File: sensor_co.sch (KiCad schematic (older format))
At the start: 2 parts

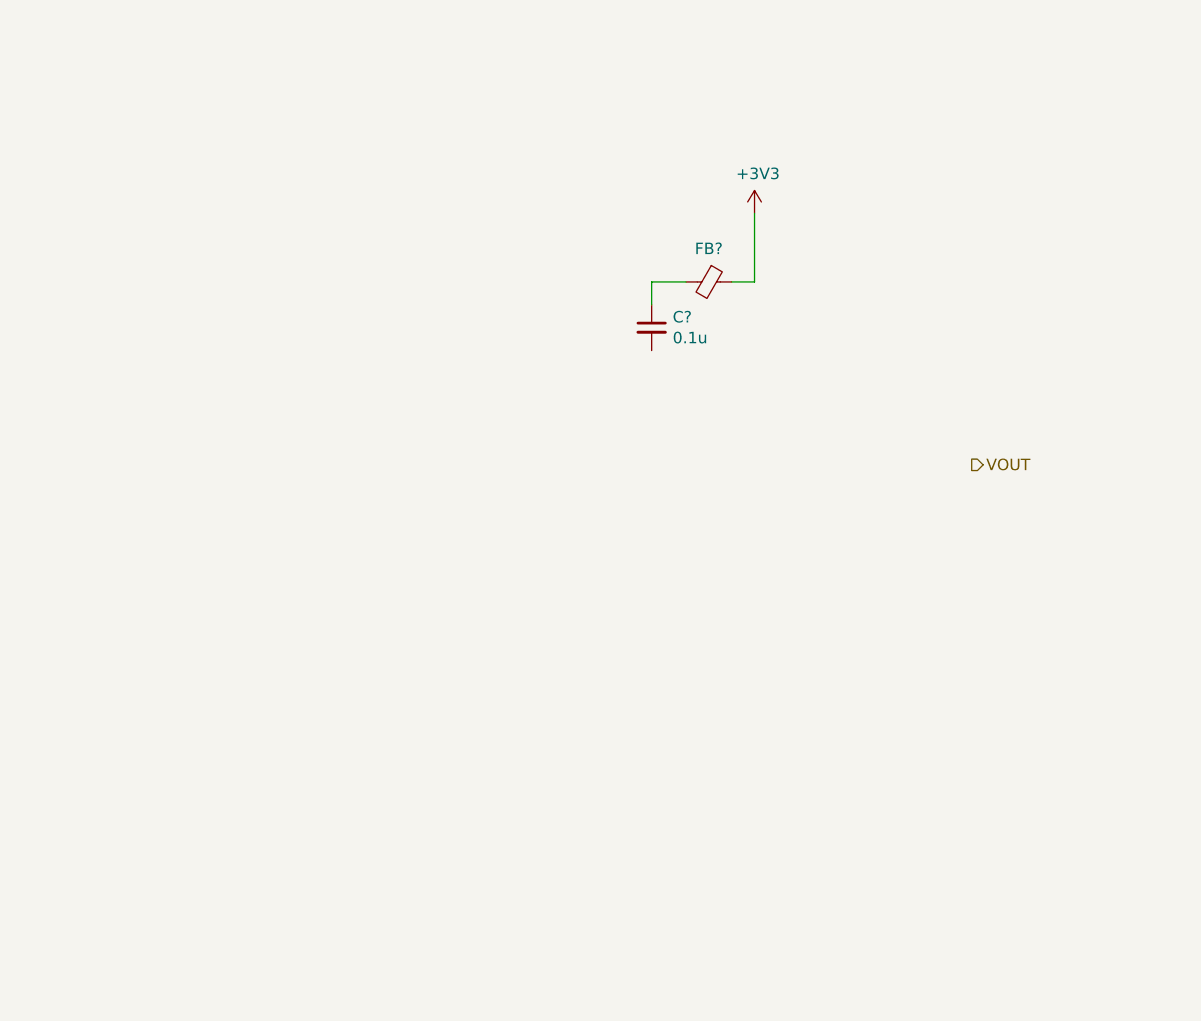
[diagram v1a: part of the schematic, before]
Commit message: Added CO sensor
Carbon Monoxide Sensor layout
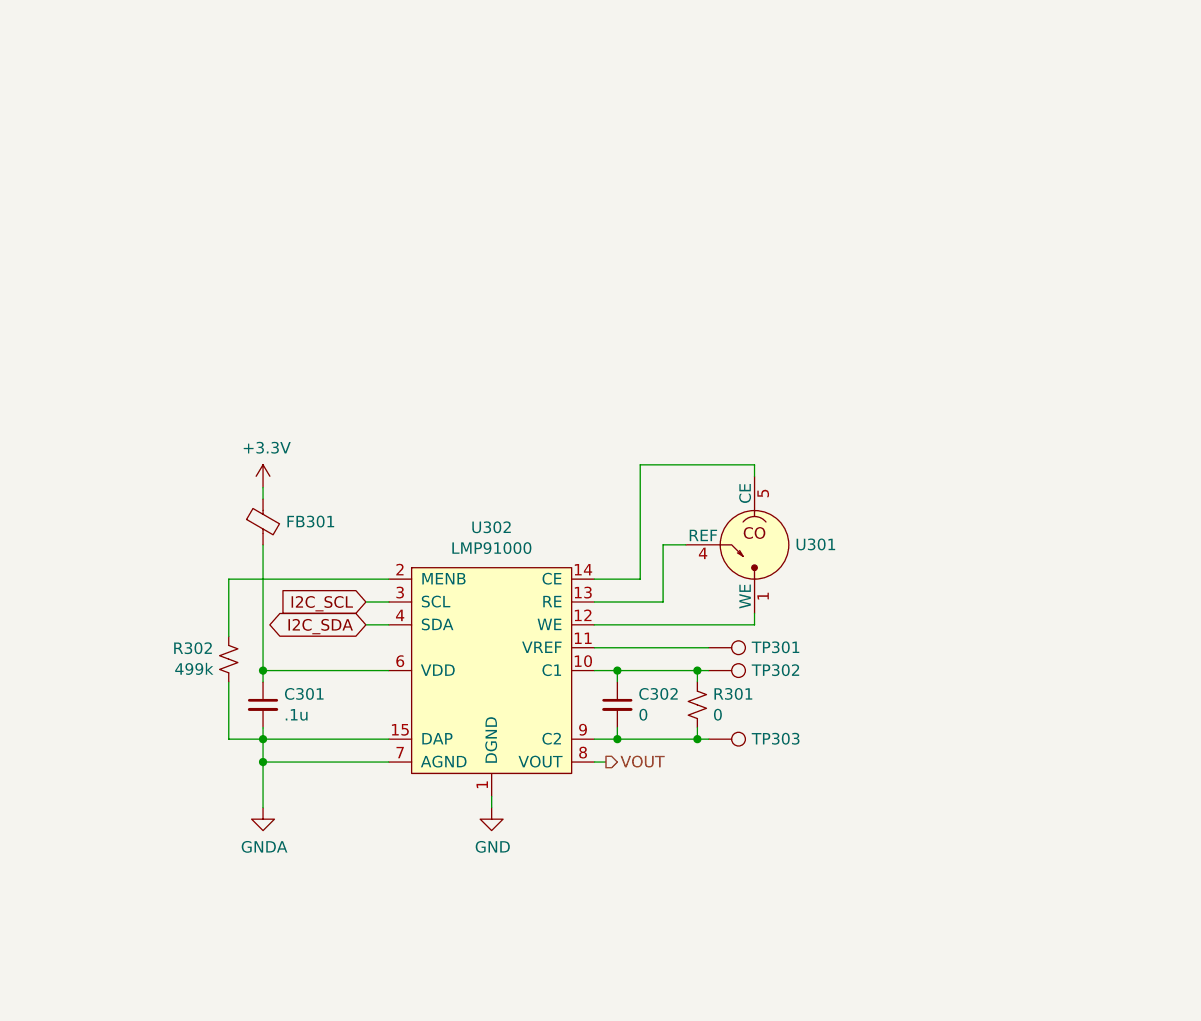
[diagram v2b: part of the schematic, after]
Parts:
- removed C?: 0.1u, Capacitor_SMD:C_0603_1608Metric, symbol Device:C_Small
- removed FB?: 470, Inductor_SMD:L_0603_1608Metric, symbol Device:Ferrite_Bead_Small
- added C301: .1u, Capacitor_SMD:C_0402_1005Metric, symbol Device:C_Small
- added C302: 0, Capacitor_SMD:C_0603_1608Metric, symbol Device:C_Small
- added FB301: Ferrite_Bead_Small, symbol Device:Ferrite_Bead_Small
- added R301: 0, Resistor_SMD:R_0603_1608Metric, symbol Device:R_Small_US
- added R302: 499k, Resistor_SMD:R_0603_1608Metric, symbol Device:R_Small_US
- added TP301, TP302, TP303: TestPoint, symbol Connector:TestPoint
- added U301: 110-102, mylib:SPEC_110-102, symbol mylib:110-102
- added U302: LMP91000, Package_SON:WSON-14-1EP_4.0x4.0mm_P0.5mm_EP2.6x2.6mm, symbol mylib:LMP91000
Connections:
- net +3V3: now also FB301.1
- net VOUT: now also U302.8 (VOUT)
- new net: C302.1, R301.1, TP302.1, U302.10 (C1)
- new net: TP301.1, U302.11 (VREF)
- new net: U301.1 (WE), U301.6 (WE), U302.12 (WE)
- new net: U301.4 (REF), U302.13 (RE)
- new net: U301.5 (CE), U302.14 (CE)
- new net: R302.1, U302.2 (MENB)
- new net: C301.1, FB301.2, U302.6 (VDD)
- new net: C302.2, R301.2, TP303.1, U302.9 (C2)
- new net: U301.2 (NC), U301.3 (NC)
- new net GND: U302.1 (DGND)
- new net GNDA: C301.2, R302.2, U302.15 (DAP), U302.7 (AGND)
- new net I2C_SCL: U302.3 (SCL)
- new net I2C_SDA: U302.4 (SDA)

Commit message: Minor part picking and annotation
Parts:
- FB301: footprint (none) -> Inductor_SMD:L_0603_1608Metric; Digikey (none) -> 490-5223-1-ND; MPN (none) -> BLM18PG471SN1D; Mouser (none) -> 81-BLM18PG471SN1D; Note (none) -> 470 Ohms @ 100MHz 1 Power Line Ferrite Bead 0603 1A 200mOhm
- TP301, TP302, TP303: DNP (none) -> 1
- U301: Digikey (none) -> 1684-1000-ND; MPN (none) -> 110-102; Manufacturer (none) -> SPEC Sensors, LLC
- U302: Digikey (none) -> 296-44382-1-ND; LCSC (none) -> C181364, C84366; MPN (none) -> LMP91000SD; Manufacturer (none) -> Texas Instruments; Note (none) -> IC AFE 1 CHAN 8BIT 14WSON
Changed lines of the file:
@@
 F 2 "Package_SON:WSON-14-1EP_4.0x4.0mm_P0.5mm_EP2.6x2.6mm" H 5600 3900 50  0001 C CNN
 F 3 "https://www.ti.com/lit/ds/symlink/lmp91000.pdf" H 5500 2950 50  0001 C CNN
+F 4 "296-44382-1-ND" H 5500 3450 50  0001 C CNN "Digikey"
+F 5 "C181364, C84366" H 5500 3450 50  0001 C CNN "LCSC"
+F 6 "LMP91000SD" H 5500 3450 50  0001 C CNN "MPN"
+F 7 "Texas Instruments" H 5500 3450 50  0001 C CNN "Manufacturer"
+F 8 "IC AFE 1 CHAN 8BIT 14WSON" H 5500 3450 50  0001 C CNN "Note"
 	1    5500 3450
 	1    0    0    -1
@@
 F 2 "mylib:SPEC_110-102" H 7150 3300 50  0001 C CNN
 F 3 "" H 6650 3100 50  0001 C CNN
+F 4 "1684-1000-ND" H 6650 3100 50  0001 C CNN "Digikey"
+F 5 "110-102" H 6650 3100 50  0001 C CNN "MPN"
+F 6 "SPEC Sensors, LLC" H 6650 3100 50  0001 C CNN "Manufacturer"
 	1    6650 3100
 	1    0    0    -1
@@
 F 2 "" H 6650 3550 50  0001 C CNN
 F 3 "~" H 6650 3550 50  0001 C CNN
+F 4 "1" H 6450 3550 50  0001 C CNN "DNP"
 	1    6450 3550
 	0    1    1    0
@@
 F 0 "FB301" H 4600 3000 50  0000 L CNN
 F 1 "Ferrite_Bead_Small" H 4600 2955 50  0001 L CNN
-F 2 "" V 4430 3000 50  0001 C CNN
+F 2 "Inductor_SMD:L_0603_1608Metric" V 4430 3000 50  0001 C CNN
 F 3 "~" H 4500 3000 50  0001 C CNN
+F 4 "490-5223-1-ND" H 4500 3000 50  0001 C CNN "Digikey"
+F 5 "BLM18PG471SN1D" H 4500 3000 50  0001 C CNN "MPN"
+F 6 "81-BLM18PG471SN1D " H 4500 3000 50  0001 C CNN "Mouser"
+F 7 "470 Ohms @ 100MHz 1 Power Line Ferrite Bead 0603 1A 200mOhm" H 4500 3000 50  0001 C CNN "Note"
 	1    4500 3000
 	1    0    0    -1
@@
 F 2 "" H 6650 3650 50  0001 C CNN
 F 3 "~" H 6650 3650 50  0001 C CNN
+F 4 "1" H 6450 3650 50  0001 C CNN "DNP"
 	1    6450 3650
 	0    1    1    0
@@
 F 2 "" H 6650 3950 50  0001 C CNN
 F 3 "~" H 6650 3950 50  0001 C CNN
+F 4 "1" H 6450 3950 50  0001 C CNN "DNP"
 	1    6450 3950
 	0    1    1    0

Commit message: Continue part picking
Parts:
- C301: value .1u -> 0.1u; footprint Capacitor_SMD:C_0402_1005Metric -> Capacitor_SMD:C_0603_1608Metric; Alt (none) -> .1u; Current (none) -> .1u; Description (none) -> .1u; Digikey 311-1336-1-ND -> 1292-1643-1-ND; Error 10% -> .1u; LCSC C129131 -> (none); MPN CC0402KRX5R6BB104 -> 0603B104K500CT; Mfr (none) -> .1u; Note CAP CER 0.1UF 10V X5R 0402 -> CAP CER 0.1UF 50V X7R 0603
- C302: DNP (none) -> 1
- FB301: LCSC (none) -> C97853
- TP301, TP302, TP303: footprint (none) -> TestPoint:TestPoint_Pad_D1.0mm
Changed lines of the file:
@@
 F 0 "TP301" V 6450 3738 50  0000 L CNN
 F 1 "TestPoint" V 6495 3738 50  0001 L CNN
-F 2 "" H 6650 3550 50  0001 C CNN
+F 2 "TestPoint:TestPoint_Pad_D1.0mm" H 6650 3550 50  0001 C CNN
 F 3 "~" H 6650 3550 50  0001 C CNN
 F 4 "1" H 6450 3550 50  0001 C CNN "DNP"
@@
 F 6 "81-BLM18PG471SN1D " H 4500 3000 50  0001 C CNN "Mouser"
 F 7 "470 Ohms @ 100MHz 1 Power Line Ferrite Bead 0603 1A 200mOhm" H 4500 3000 50  0001 C CNN "Note"
+F 8 "C97853" H 4500 3000 50  0001 C CNN "LCSC"
 	1    4500 3000
 	1    0    0    -1
@@
 P 4500 3800
 F 0 "C301" H 4592 3846 50  0000 L CNN
-F 1 ".1u" H 4592 3755 50  0000 L CNN
-F 2 "Capacitor_SMD:C_0402_1005Metric" H 4500 3800 50  0001 C CNN
-F 3 "~" H 4500 3800 50  0001 C CNN
-F 4 "311-1336-1-ND" H 4500 3800 50  0001 C CNN "Digikey"
-F 5 "10%" H 4500 3800 50  0001 C CNN "Error"
-F 6 "C129131" H 4500 3800 50  0001 C CNN "LCSC"
-F 7 "CC0402KRX5R6BB104" H 4500 3800 50  0001 C CNN "MPN"
-F 8 "CAP CER 0.1UF 10V X5R 0402" H 4500 3800 50  0001 C CNN "Note"
+F 1 "0.1u" H 4592 3755 50  0000 L CNN
+F 2 "Capacitor_SMD:C_0603_1608Metric" H 4500 3800 50  0001 C CNN
+F 3 ".1u" H 4500 3800 50  0001 C CNN
+F 4 "1292-1643-1-ND" H 4500 3800 50  0001 C CNN "Digikey"
+F 5 ".1u" H 4500 3800 50  0001 C CNN "Error"
+F 6 "" H 4500 3800 50  0001 C CNN "LCSC"
+F 7 "0603B104K500CT" H 4500 3800 50  0001 C CNN "MPN"
+F 8 "CAP CER 0.1UF 50V X7R 0603" H 4500 3800 50  0001 C CNN "Note"
+F 9 ".1u" H 4500 3800 50  0001 C CNN "Alt"
+F 10 ".1u" H 4500 3800 50  0001 C CNN "Current"
+F 11 ".1u" H 4500 3800 50  0001 C CNN "Description"
+F 12 ".1u" H 4500 3800 50  0001 C CNN "Mfr"
 	1    4500 3800
 	1    0    0    -1
@@
 F 0 "TP302" V 6450 3838 50  0000 L CNN
 F 1 "TestPoint" V 6495 3838 50  0001 L CNN
-F 2 "" H 6650 3650 50  0001 C CNN
+F 2 "TestPoint:TestPoint_Pad_D1.0mm" H 6650 3650 50  0001 C CNN
 F 3 "~" H 6650 3650 50  0001 C CNN
 F 4 "1" H 6450 3650 50  0001 C CNN "DNP"
@@
 F 0 "TP303" V 6450 4138 50  0000 L CNN
 F 1 "TestPoint" V 6495 4138 50  0001 L CNN
-F 2 "" H 6650 3950 50  0001 C CNN
+F 2 "TestPoint:TestPoint_Pad_D1.0mm" H 6650 3950 50  0001 C CNN
 F 3 "~" H 6650 3950 50  0001 C CNN
 F 4 "1" H 6450 3950 50  0001 C CNN "DNP"
@@
 F 2 "Capacitor_SMD:C_0603_1608Metric" H 6050 3800 50  0001 C CNN
 F 3 "~" H 6050 3800 50  0001 C CNN
+F 4 "1" H 6050 3800 50  0001 C CNN "DNP"
 	1    6050 3800
 	1    0    0    -1

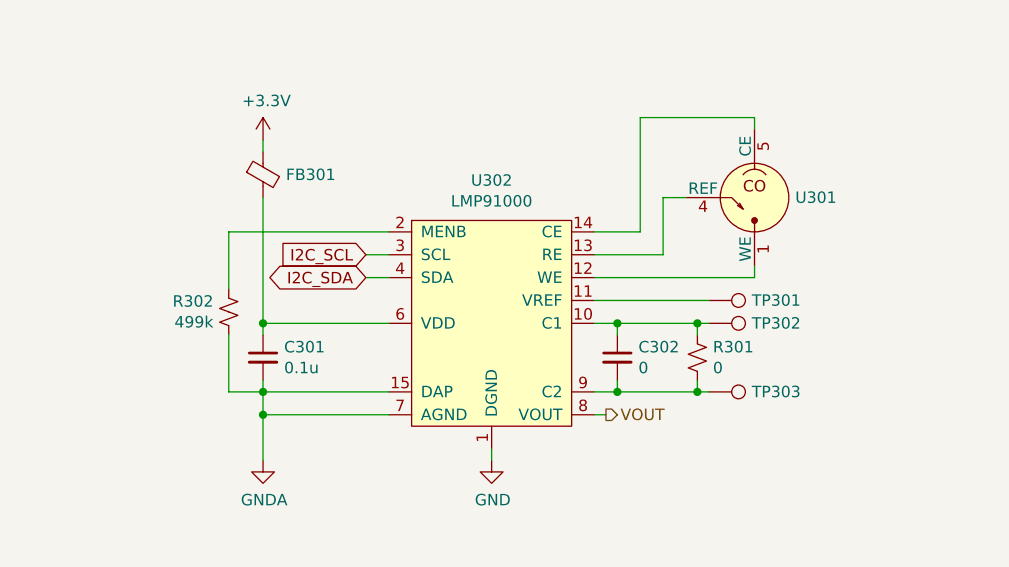
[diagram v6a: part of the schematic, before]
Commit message: Re-annotate all parts
Cleans up annotations
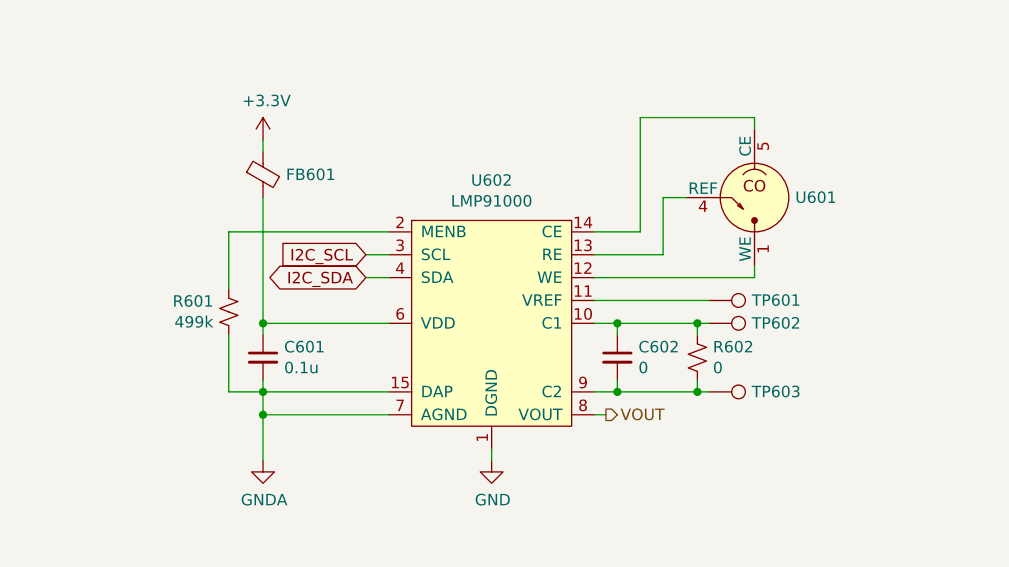
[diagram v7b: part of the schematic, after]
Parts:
- renumbered C301 to C601, C302 to C602, FB301 to FB601, R302 to R601, R301 to R602, TP301 to TP601, TP302 to TP602, TP303 to TP603, U301 to U601, U302 to U602
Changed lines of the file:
@@
 1) No external bias required for CO, thus no accurate bias source for ic
 $Comp
-L mylib:LMP91000 U302
+L mylib:LMP91000 U602
 U 1 1 5F98A650
 P 5500 3450
-F 0 "U302" H 5500 3875 50  0000 C CNN
+F 0 "U602" H 5500 3875 50  0000 C CNN
 F 1 "LMP91000" H 5500 3784 50  0000 C CNN
 F 2 "Package_SON:WSON-14-1EP_4.0x4.0mm_P0.5mm_EP2.6x2.6mm" H 5600 3900 50  0001 C CNN
@@
 $EndComp
 $Comp
-L mylib:110-102 U301
+L mylib:110-102 U601
 U 1 1 5F98B02A
 P 6650 3100
-F 0 "U301" H 6828 3100 50  0000 L CNN
+F 0 "U601" H 6828 3100 50  0000 L CNN
 F 1 "110-102" H 6950 3400 50  0001 C CNN
 F 2 "mylib:SPEC_110-102" H 7150 3300 50  0001 C CNN
@@
 	5950 3550 6450 3550
 $Comp
-L Connector:TestPoint TP301
+L Connector:TestPoint TP601
 U 1 1 5F98CA68
 P 6450 3550
-F 0 "TP301" V 6450 3738 50  0000 L CNN
+F 0 "TP601" V 6450 3738 50  0000 L CNN
 F 1 "TestPoint" V 6495 3738 50  0001 L CNN
 F 2 "TestPoint:TestPoint_Pad_D1.0mm" H 6650 3550 50  0001 C CNN
@@
 	5950 4050 6000 4050
 $Comp
-L Device:Ferrite_Bead_Small FB301
+L Device:Ferrite_Bead_Small FB601
 U 1 1 5F991181
 P 4500 3000
-F 0 "FB301" H 4600 3000 50  0000 L CNN
+F 0 "FB601" H 4600 3000 50  0000 L CNN
 F 1 "Ferrite_Bead_Small" H 4600 2955 50  0001 L CNN
 F 2 "Inductor_SMD:L_0603_1608Metric" V 4430 3000 50  0001 C CNN
@@
 	4500 3650 5050 3650
 $Comp
-L Device:C_Small C301
+L Device:C_Small C601
 U 1 1 5F991BC7
 P 4500 3800
-F 0 "C301" H 4592 3846 50  0000 L CNN
+F 0 "C601" H 4592 3846 50  0000 L CNN
 F 1 "0.1u" H 4592 3755 50  0000 L CNN
 F 2 "Capacitor_SMD:C_0603_1608Metric" H 4500 3800 50  0001 C CNN
@@
 Connection ~ 4500 3650
 $Comp
-L power:+3.3V #PWR0301
+L power:+3.3V #PWR0601
 U 1 1 5F99228C
 P 4500 2850
-F 0 "#PWR0301" H 4500 2700 50  0001 C CNN
+F 0 "#PWR0601" H 4500 2700 50  0001 C CNN
 F 1 "+3.3V" H 4515 3023 50  0000 C CNN
 F 2 "" H 4500 2850 50  0001 C CNN
@@
 $EndComp
 $Comp
-L power:GNDA #PWR0302
+L power:GNDA #PWR0602
 U 1 1 5F992930
 P 4500 4250
-F 0 "#PWR0302" H 4500 4000 50  0001 C CNN
+F 0 "#PWR0602" H 4500 4000 50  0001 C CNN
 F 1 "GNDA" H 4505 4077 50  0000 C CNN
 F 2 "" H 4500 4250 50  0001 C CNN
@@
 	4500 4050 4500 4250
 $Comp
-L power:GND #PWR0303
+L power:GND #PWR0603
 U 1 1 5F9966DB
 P 5500 4250
-F 0 "#PWR0303" H 5500 4000 50  0001 C CNN
+F 0 "#PWR0603" H 5500 4000 50  0001 C CNN
 F 1 "GND" H 5505 4077 50  0000 C CNN
 F 2 "" H 5500 4250 50  0001 C CNN
@@
 	5500 4200 5500 4250
 $Comp
-L Connector:TestPoint TP302
+L Connector:TestPoint TP602
 U 1 1 5F998986
 P 6450 3650
-F 0 "TP302" V 6450 3838 50  0000 L CNN
+F 0 "TP602" V 6450 3838 50  0000 L CNN
 F 1 "TestPoint" V 6495 3838 50  0001 L CNN
 F 2 "TestPoint:TestPoint_Pad_D1.0mm" H 6650 3650 50  0001 C CNN
@@
 $EndComp
 $Comp
-L Connector:TestPoint TP303
+L Connector:TestPoint TP603
 U 1 1 5F999953
 P 6450 3950
-F 0 "TP303" V 6450 4138 50  0000 L CNN
+F 0 "TP603" V 6450 4138 50  0000 L CNN
 F 1 "TestPoint" V 6495 4138 50  0001 L CNN
 F 2 "TestPoint:TestPoint_Pad_D1.0mm" H 6650 3950 50  0001 C CNN
@@
 $EndComp
 $Comp
-L Device:R_Small_US R301
+L Device:R_Small_US R602
 U 1 1 5F9B2366
 P 6400 3800
-F 0 "R301" H 6468 3846 50  0000 L CNN
+F 0 "R602" H 6468 3846 50  0000 L CNN
 F 1 "0" H 6468 3755 50  0000 L CNN
 F 2 "Resistor_SMD:R_0603_1608Metric" H 6400 3800 50  0001 C CNN
@@
 	4500 3100 4500 3650
 $Comp
-L Device:C_Small C302
+L Device:C_Small C602
 U 1 1 5F9B1AD5
 P 6050 3800
-F 0 "C302" H 6142 3846 50  0000 L CNN
+F 0 "C602" H 6142 3846 50  0000 L CNN
 F 1 "0" H 6142 3755 50  0000 L CNN
 F 2 "Capacitor_SMD:C_0603_1608Metric" H 6050 3800 50  0001 C CNN
@@
 Connection ~ 6400 3650
 $Comp
-L Device:R_Small_US R302
+L Device:R_Small_US R601
 U 1 1 5F9CC547
 P 4350 3600
-F 0 "R302" H 4283 3646 50  0000 R CNN
+F 0 "R601" H 4283 3646 50  0000 R CNN
 F 1 "499k" H 4283 3555 50  0000 R CNN
 F 2 "Resistor_SMD:R_0603_1608Metric" H 4350 3600 50  0001 C CNN

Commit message: Prefinal, layout done
Update FB to use inductor footprints
DNP net tie
Update diode symbol in power
Add battery voltage divider in power
Supply 5V power to aux sensor connector
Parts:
- R601: symbol Device:R_Small_US -> Device:R_US
- R602: DNP (none) -> 1
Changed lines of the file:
@@
 F 2 "Resistor_SMD:R_0603_1608Metric" H 6400 3800 50  0001 C CNN
 F 3 "~" H 6400 3800 50  0001 C CNN
+F 4 "1" H 6400 3800 50  0001 C CNN "DNP"
 	1    6400 3800
 	1    0    0    -1
@@
 Connection ~ 6400 3650
 $Comp
-L Device:R_Small_US R601
+L Device:R_US R601
 U 1 1 5F9CC547
 P 4350 3600
@@
 $EndComp
 Wire Wire Line
-	4350 3250 4350 3500
+	4350 3250 4350 3450
 Wire Wire Line
-	4350 3700 4350 3950
+	4350 3750 4350 3950
 $EndSCHEMATC
